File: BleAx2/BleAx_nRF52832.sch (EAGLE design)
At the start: 41 parts, among them CN1 6p-2.54, J1 2.0MM-90D, J5 MICROUSB, U1 NRF52832, U2 MCP73832T-2ACI/OT-SOT23-5, U4 MIC5225-3.3, X1 32MHz, X2 32.768kHz

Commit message: evolve
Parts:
- added U$1: 1,1/0,6, wirepad:1,1/0,6
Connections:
- new net LIS_CS: U1.P0.09/NFC1@11, U3.CS
- new net LIS_INT1: U$1.P, U1.P0.10/NFC2@12, U3.INT1
- new net MISO_01: U1.P0.08@10, U3.SDO_SA0
- new net MOSI_01: U1.P0.07@09, U3.SDA_SDI_SDO
- new net SCK_01: U1.P0.06@08, U3.SCL_SPC
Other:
- moved on the sheet: C13, C6
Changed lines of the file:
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@@
 <part name="J1" library="Seeed-OPL-Connector" deviceset="CONN-HEADER-PH-SIDE-(2P-2.0MM)" device="'90D'" value="2.0MM-90D"/>
 <part name="VDD_BATT1" library="supply2" deviceset="VCC" device="" value="VDD_BATT"/>
+<part name="U$1" library="wirepad" deviceset="1,1/0,6" device=""/>
 </parts>
 <sheets>
@@
 <instance part="C12" gate="C$1" x="27.94" y="96.52" rot="R90"/>
 <instance part="U3" gate="G$1" x="43.18" y="45.72"/>
-<instance part="GND8" gate="1" x="7.62" y="38.1" rot="MR0"/>
-<instance part="VDD_NRF7" gate="G$1" x="7.62" y="55.88"/>
-<instance part="C6" gate="C$1" x="7.62" y="48.26"/>
+<instance part="GND8" gate="1" x="7.62" y="48.26" rot="MR0"/>
+<instance part="VDD_NRF7" gate="G$1" x="7.62" y="68.58"/>
+<instance part="C6" gate="C$1" x="7.62" y="58.42"/>
 <instance part="VDD_NRF8" gate="G$1" x="45.72" y="68.58"/>
 <instance part="GND11" gate="1" x="63.5" y="53.34" rot="MR180"/>
 <instance part="GND12" gate="1" x="22.86" y="58.42" rot="MR180"/>
 <instance part="CN1" gate="G$1" x="177.8" y="49.53"/>
-<instance part="GND13" gate="1" x="15.24" y="38.1" rot="MR0"/>
-<instance part="C13" gate="C$1" x="15.24" y="48.26"/>
+<instance part="GND13" gate="1" x="12.7" y="40.64" rot="MR0"/>
+<instance part="C13" gate="C$1" x="12.7" y="50.8"/>
+<instance part="U$1" gate="G$1" x="86.36" y="68.58" rot="R90"/>
 </instances>
 <busses>
@@
 <segment>
 <pinref part="GND8" gate="1" pin="GND"/>
-<wire x1="7.62" y1="40.64" x2="7.62" y2="43.18" width="0.1524" layer="91"/>
+<wire x1="7.62" y1="50.8" x2="7.62" y2="53.34" width="0.1524" layer="91"/>
 <pinref part="C6" gate="C$1" pin="2"/>
 </segment>
@@
 <segment>
 <pinref part="GND13" gate="1" pin="GND"/>
-<wire x1="15.24" y1="40.64" x2="15.24" y2="43.18" width="0.1524" layer="91"/>
+<wire x1="12.7" y1="43.18" x2="12.7" y2="45.72" width="0.1524" layer="91"/>
 <pinref part="C13" gate="C$1" pin="2"/>
 </segment>
@@
 </segment>
 <segment>
-<wire x1="7.62" y1="53.34" x2="7.62" y2="50.8" width="0.1524" layer="91"/>
+<wire x1="7.62" y1="66.04" x2="7.62" y2="60.96" width="0.1524" layer="91"/>
 <pinref part="VDD_NRF7" gate="G$1" pin="VCC"/>
-<wire x1="27.94" y1="53.34" x2="15.24" y2="53.34" width="0.1524" layer="91"/>
-<junction x="7.62" y="53.34"/>
+<junction x="7.62" y="66.04"/>
 <pinref part="C6" gate="C$1" pin="1"/>
+<wire x1="12.7" y1="66.04" x2="7.62" y2="66.04" width="0.1524" layer="91"/>
+<wire x1="12.7" y1="66.04" x2="12.7" y2="53.34" width="0.1524" layer="91"/>
+<pinref part="C13" gate="C$1" pin="1"/>
 <pinref part="U3" gate="G$1" pin="VDDIO"/>
-<wire x1="15.24" y1="53.34" x2="7.62" y2="53.34" width="0.1524" layer="91"/>
-<wire x1="15.24" y1="53.34" x2="15.24" y2="50.8" width="0.1524" layer="91"/>
-<label x="15.24" y="53.34" size="1.778" layer="95"/>
-<pinref part="C13" gate="C$1" pin="1"/>
-<junction x="15.24" y="53.34"/>
+<wire x1="27.94" y1="53.34" x2="25.4" y2="53.34" width="0.1524" layer="91"/>
+<wire x1="25.4" y1="53.34" x2="25.4" y2="66.04" width="0.1524" layer="91"/>
+<wire x1="25.4" y1="66.04" x2="12.7" y2="66.04" width="0.1524" layer="91"/>
+<junction x="12.7" y="66.04"/>
 </segment>
 </net>
@@
 </segment>
 </net>
+<net name="MISO_01" class="0">
+<segment>
+<pinref part="U3" gate="G$1" pin="SDO_SA0"/>
+<wire x1="27.94" y1="38.1" x2="22.86" y2="38.1" width="0.1524" layer="91"/>
+<wire x1="22.86" y1="38.1" x2="22.86" y2="25.4" width="0.1524" layer="91"/>
+<wire x1="22.86" y1="25.4" x2="15.24" y2="25.4" width="0.1524" layer="91"/>
+<label x="15.24" y="25.4" size="1.27" layer="95" rot="R180" xref="yes"/>
+</segment>
+<segment>
+<wire x1="88.9" y1="78.74" x2="76.2" y2="78.74" width="0.1524" layer="91"/>
+<label x="76.2" y="78.74" size="1.27" layer="95" rot="R180" xref="yes"/>
+<pinref part="U1" gate="U$1" pin="P0.08@10"/>
+</segment>
+</net>
+<net name="SCK_01" class="0">
+<segment>
+<pinref part="U3" gate="G$1" pin="SCL_SPC"/>
+<wire x1="27.94" y1="45.72" x2="17.78" y2="45.72" width="0.1524" layer="91"/>
+<wire x1="17.78" y1="45.72" x2="17.78" y2="30.48" width="0.1524" layer="91"/>
+<wire x1="17.78" y1="30.48" x2="15.24" y2="30.48" width="0.1524" layer="91"/>
+<label x="15.24" y="30.48" size="1.27" layer="95" rot="R180" xref="yes"/>
+</segment>
+<segment>
+<wire x1="76.2" y1="83.82" x2="88.9" y2="83.82" width="0.1524" layer="91"/>
+<label x="76.2" y="83.82" size="1.27" layer="95" rot="R180" xref="yes"/>
+<pinref part="U1" gate="U$1" pin="P0.06@08"/>
+</segment>
+</net>
+<net name="MOSI_01" class="0">
+<segment>
+<pinref part="U3" gate="G$1" pin="SDA_SDI_SDO"/>
+<wire x1="27.94" y1="40.64" x2="20.32" y2="40.64" width="0.1524" layer="91"/>
+<wire x1="20.32" y1="40.64" x2="20.32" y2="27.94" width="0.1524" layer="91"/>
+<wire x1="20.32" y1="27.94" x2="15.24" y2="27.94" width="0.1524" layer="91"/>
+<label x="15.24" y="27.94" size="1.27" layer="95" rot="R180" xref="yes"/>
+</segment>
+<segment>
+<wire x1="76.2" y1="81.28" x2="88.9" y2="81.28" width="0.1524" layer="91"/>
+<label x="76.2" y="81.28" size="1.27" layer="95" rot="R180" xref="yes"/>
+<pinref part="U1" gate="U$1" pin="P0.07@09"/>
+</segment>
+</net>
+<net name="LIS_CS" class="0">
+<segment>
+<pinref part="U3" gate="G$1" pin="CS"/>
+<wire x1="27.94" y1="35.56" x2="25.4" y2="35.56" width="0.1524" layer="91"/>
+<wire x1="25.4" y1="35.56" x2="25.4" y2="22.86" width="0.1524" layer="91"/>
+<wire x1="25.4" y1="22.86" x2="15.24" y2="22.86" width="0.1524" layer="91"/>
+<label x="15.24" y="22.86" size="1.27" layer="95" rot="R180" xref="yes"/>
+</segment>
+<segment>
+<wire x1="88.9" y1="76.2" x2="76.2" y2="76.2" width="0.1524" layer="91"/>
+<label x="76.2" y="76.2" size="1.27" layer="95" rot="R180" xref="yes"/>
+<pinref part="U1" gate="U$1" pin="P0.09/NFC1@11"/>
+</segment>
+</net>
+<net name="LIS_INT1" class="0">
+<segment>
+<pinref part="U3" gate="G$1" pin="INT1"/>
+<wire x1="58.42" y1="45.72" x2="63.5" y2="45.72" width="0.1524" layer="91"/>
+<label x="63.5" y="45.72" size="1.27" layer="95" xref="yes"/>
+</segment>
+<segment>
+<label x="76.2" y="73.66" size="1.27" layer="95" rot="R180" xref="yes"/>
+<wire x1="76.2" y1="73.66" x2="86.36" y2="73.66" width="0.1524" layer="91"/>
+<pinref part="U$1" gate="G$1" pin="P"/>
+<wire x1="86.36" y1="71.12" x2="86.36" y2="73.66" width="0.1524" layer="91"/>
+<junction x="86.36" y="73.66"/>
+<pinref part="U1" gate="U$1" pin="P0.10/NFC2@12"/>
+<wire x1="86.36" y1="73.66" x2="88.9" y2="73.66" width="0.1524" layer="91"/>
+</segment>
+</net>

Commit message: sst26
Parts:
- added U$2: SST26VF, sst26:SST26VF
- R1: value 2K -> 3K
- R10, R11: value 330R -> 1k
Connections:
- new net MISO_02: U$2.SO_SIO1, U1.P0.12@15
- new net MOSI_02: U$2.SI_SIO0, U1.P0.13@16
- new net SCK_02: U$2.SCK, U1.P0.14@17
- new net SST26_CE: U$2.!CE, U1.P0.11@14
- net GND: now also U$2.VSS
- net VCC: no longer CN1.1
- net VDD_P3V3: now also CN1.1, U$2.!WP!_SIO2, U$2.HOLD_SIO3, U$2.VDD
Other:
- moved on the sheet: C13, C6, U3

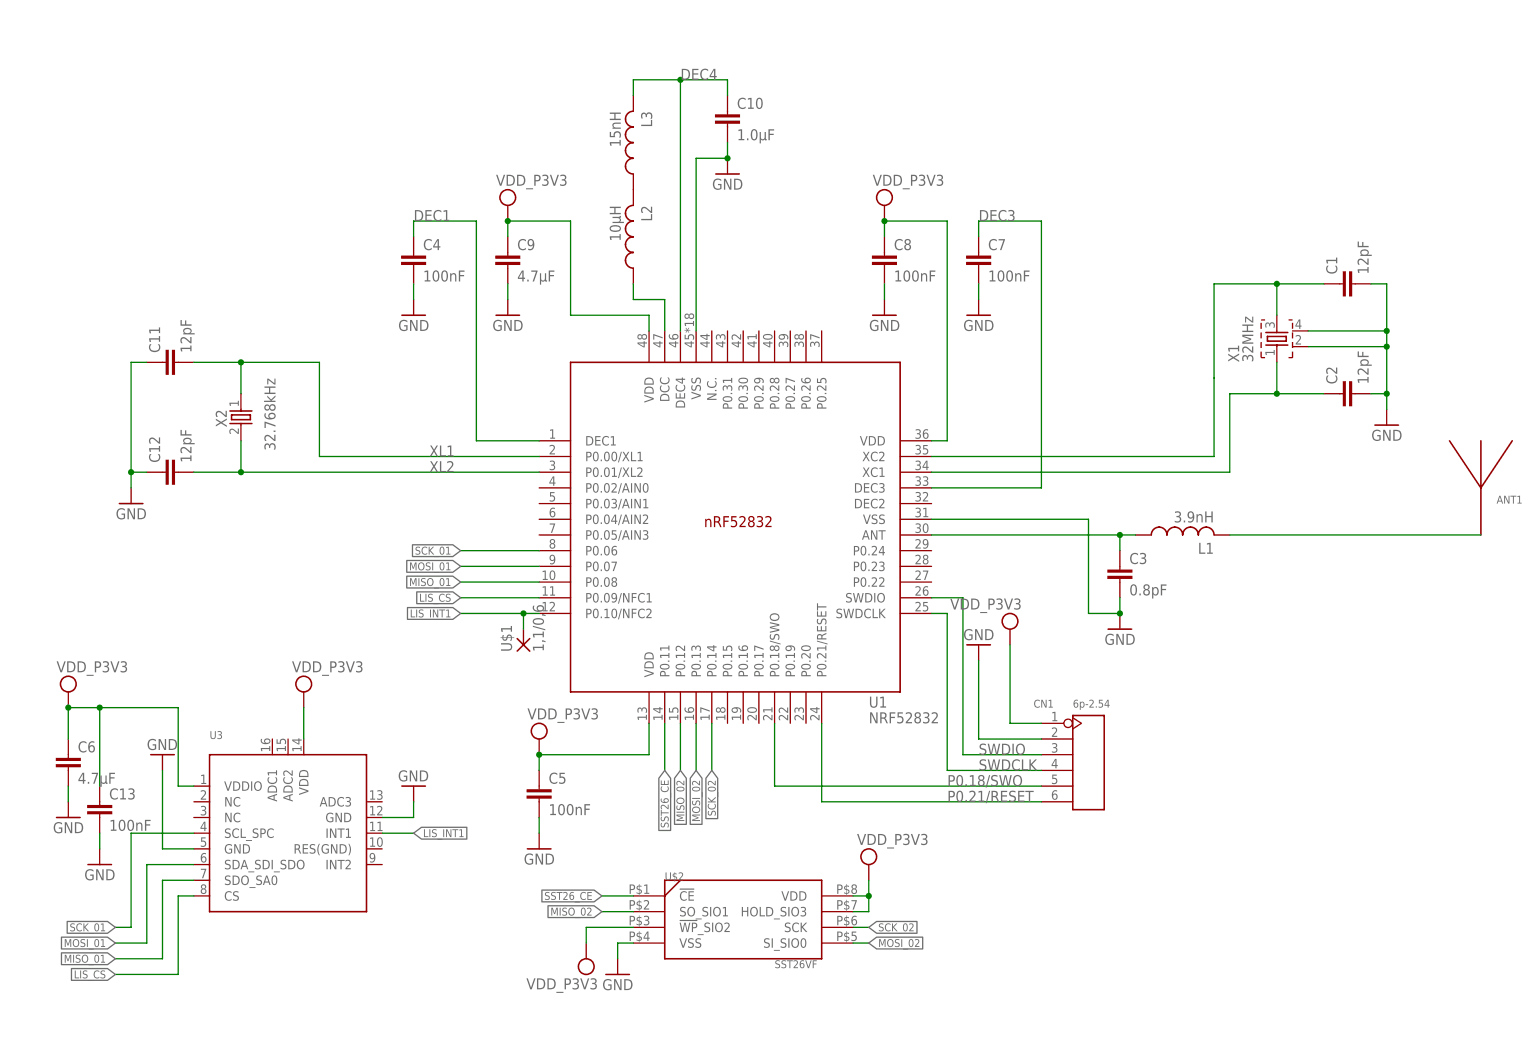
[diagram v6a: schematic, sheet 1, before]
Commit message: evolving pads added
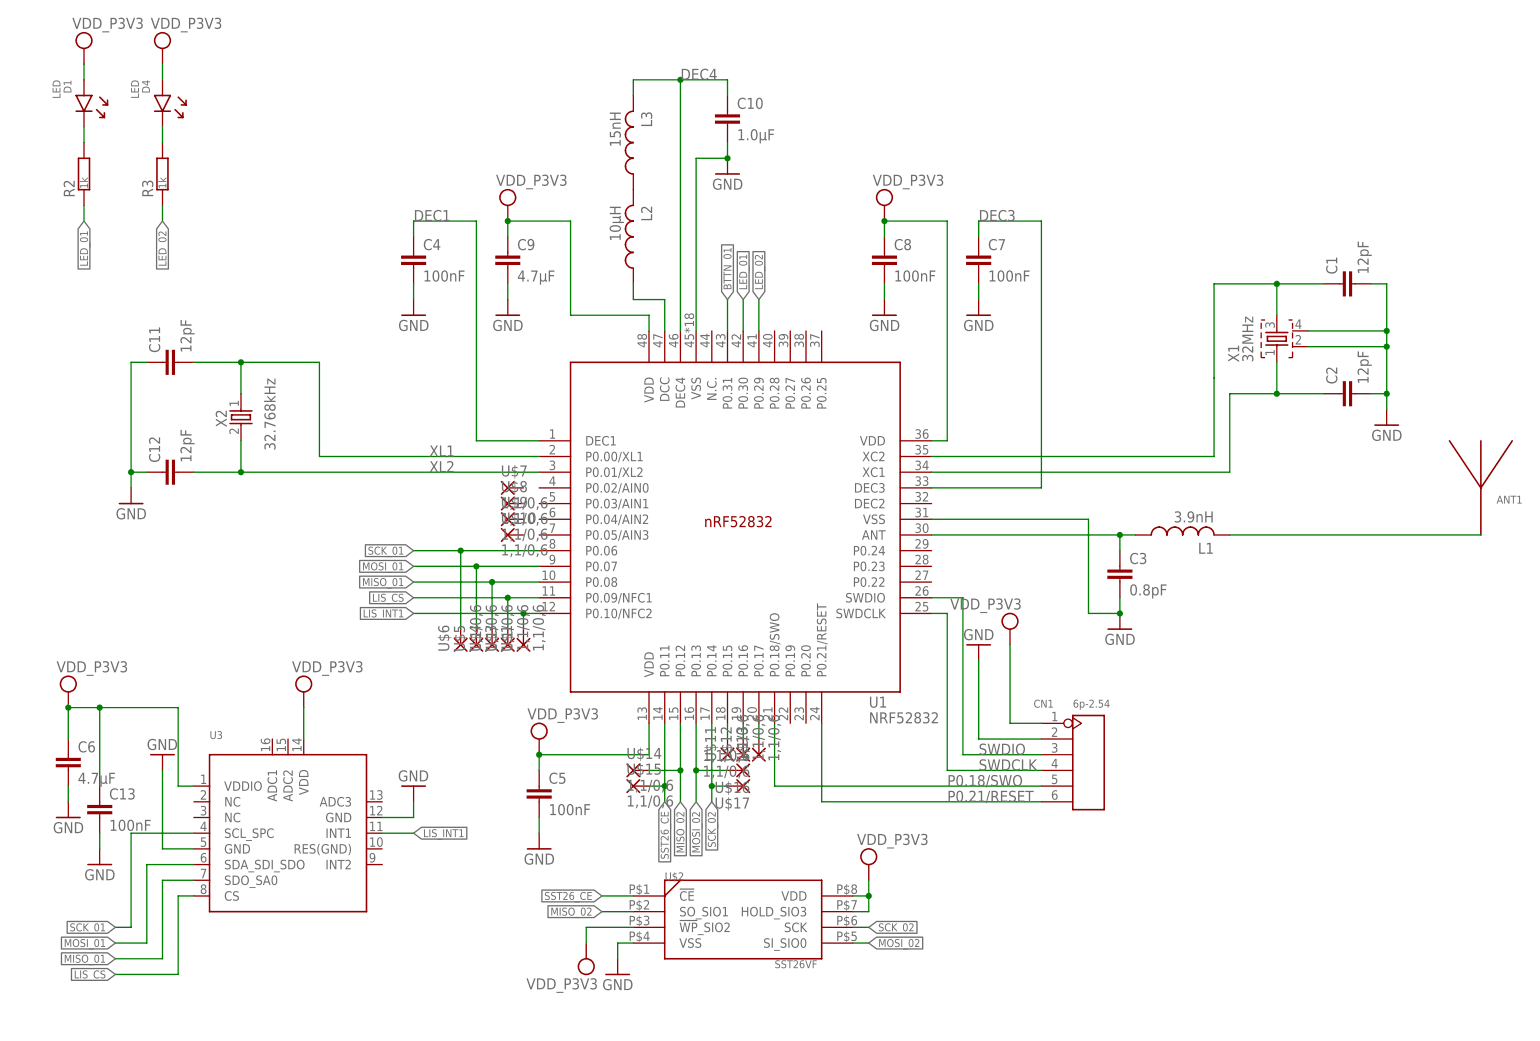
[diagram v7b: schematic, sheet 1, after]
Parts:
- removed D2: LED, Nordic_misc:LED
- removed R10: 1k, Nordic_misc:RESISTOR_0402_N
- added D1, D4: LED, Nordic_misc:LED
- added R2, R3: 1k, Nordic_misc:RESISTOR_0402_N
- added U$10, U$11, U$12, U$13, U$14, U$15, U$16, U$17, U$3, U$4, U$5, U$6, U$7, U$8, U$9: 1,1/0,6, wirepad:1,1/0,6
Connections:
- removed net P0.08: R5.1
- new net BTTN_01: R5.1, U1.P0.31@43
- new net LED_01: R2.1, U1.P0.30@42
- new net LED_02: R3.1, U1.P0.29@41
- new net N$11: D1.C, R2.2
- new net N$12: D4.C, R3.2
- new net N$13: U$12.P, U1.P0.16@19
- new net N$14: U$13.P, U1.P0.17@20
- net LIS_CS: now also U$3.P
- net MISO_01: now also U$4.P
- net MISO_02: now also U$14.P
- net MOSI_01: now also U$5.P
- net MOSI_02: now also U$16.P
- net N$8: now also U$11.P, U1.P0.15@18; no longer D2.C, R10.2
- net SCK_01: now also U$6.P
- net SCK_02: now also U$17.P
- net SST26_CE: now also U$15.P
- net VDD_P3V3: now also D1.A, D4.A; no longer D2.A

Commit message: last today
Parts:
- removed U$10, U$9: 1,1/0,6, wirepad:1,1/0,6
- removed X1: 32MHz, Nordic_nRF:XTAL_32MHZ
- added Q1: 32MHz, crystal:CRYSTALHC49S
- added Q2: 32MHz, crystal-geyer_V1_0:KX-9A
- added Q3: (no value), crystal:CRYSTALTC38H
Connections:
- removed net GND@2: U3.GND@2
- removed net VCC: U3.VDD
- new net N$15: U$7.P, U1.P0.02/AIN0@04
- new net N$16: U$8.P, U1.P0.03/AIN1@05
- net GND: now also U3.GND@2, U3.RES(GND); no longer X1.2, X1.4
- net N$3: now also Q1.2, Q2.2; no longer X1.3
- net VDD_P3V3: now also U3.VDD
- net X1: now also Q1.1, Q2.1; no longer X1.1
- net XL1: now also Q3.1
- net XL2: now also Q3.2
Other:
- moved on the sheet: ANT1, C1, C2, C7, U$2
